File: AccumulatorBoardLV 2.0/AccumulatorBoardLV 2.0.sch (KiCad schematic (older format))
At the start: 66 parts, among them J1 Contactor 1, J10 To HV Board, J11 IMD Reset, J12 TS Interlock, J13 Temp Reset, J14 To ECU, J15 Charger LV, J16 Charger Interlock, J17 Lid Interlock, J18 From HV Board, J19 Chip 1, J2 Contactor 2, J20 Chip 2, J21 Chip 3, J22 Chip 4, J3 IMD LV, J4 BMS Connector 1, J5 BMS Connector 2, J6 BMS TX, J7 BMS RX, J8 Current Sensor, J9 BMS Reset, U1 DE1A1B-L2-12V, U10 MCP3008, U11 ISO1050, U12 stm_nucleo_FK303K8, U13 MCP3008, U14 MCP3008, U2 LM555N, U3 SN754410, U4 DE1A1B-L2-12V, U5 L78S05CV-DG, U6 DE1A1B-L2-12V, U7 DK1A1B-12V, U8 ADUM4154ARIZ, U9 MCP3008

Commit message: Began BMS slave board
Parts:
- removed C10, C11, C12, C13: 1uF, Capacitors_SMD:C_0805_HandSoldering, symbol Device:C
- removed J19: Chip 1, Connectors_Molex:Molex_NanoFit_2x05x2.50mm_Straight, symbol Connector:Conn_01x10_Male
- removed J20: Chip 2, Connectors_Molex:Molex_NanoFit_2x05x2.50mm_Straight, symbol Conn_01x10
- removed J21: Chip 3, Connectors_Molex:Molex_NanoFit_2x05x2.50mm_Straight, symbol Connector:Conn_01x10_Male
- removed J22: Chip 4, Connectors_Molex:Molex_NanoFit_2x05x2.50mm_Straight, symbol Conn_01x10
- removed R4, R5, R7, R8: R, Resistors_SMD:R_0805_HandSoldering, symbol Device:R
- removed U10, U13, U14: MCP3008, Housings_SOIC:SOIC-16_3.9x9.9mm_Pitch1.27mm, symbol MCP3008
- removed U8: ADUM4154ARIZ, Housings_SOIC:SOIC-20W_7.5x12.8mm_Pitch1.27mm, symbol FS_FINAL:ADUM4154ARIZ
- removed U9: MCP3008, Housings_SOIC:SOIC-16_3.9x9.9mm_Pitch1.27mm, symbol Analog_ADC:MCP3008
- added U?: LTC6820, symbol FS_FINAL:LTC6820
- J14: symbol Conn_01x14 -> Connector:Conn_01x14_Male
- J15: symbol Conn_01x08 -> Connector:Conn_01x08_Male
- J4: symbol Conn_01x06 -> Connector:Conn_01x06_Male
- J5: symbol Conn_01x12 -> Connector:Conn_01x12_Male
- J8: symbol Conn_01x03 -> Connector:Conn_01x03_Male
- U5: symbol L78S05CV-DG -> FS_FINAL:L78S05CV-DG
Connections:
- net labels removed: 3.3V, SCLK, TEMP_SSI, TEMP_SSO, TEMP_SS_0, TEMP_SS_1, TEMP_SS_2, TEMP_SS_3
- wire segments 88 -> 37
- no-connect marks 17 -> 8
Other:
- moved on the sheet: C6, C8, C9, J6, J7, R6, U11, U12

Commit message: updated the things
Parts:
- removed C7: 0.1uF, Capacitors_THT:C_Disc_D3.0mm_W1.6mm_P2.50mm, symbol Device:C
- removed D1, D2: D, Diodes_SMD:D_1206, symbol Device:D
- removed J13: Temp Reset, Connectors_Molex:Molex_NanoFit_1x02x2.50mm_Straight, symbol Connector:Conn_01x02_Male
- removed J18: From HV Board, Connectors_Molex:Molex_NanoFit_1x02x2.50mm_Straight, symbol Connector:Conn_01x02_Male
- removed J4: BMS Connector 1, Connectors_Molex:Molex_NanoFit_2x03x2.50mm_Straight, symbol Connector:Conn_01x06_Male
- removed J5: BMS Connector 2, Connectors_Molex:Molex_NanoFit_2x06x2.50mm_Straight, symbol Connector:Conn_01x12_Male
- removed J6: BMS TX, Connectors_Molex:Molex_NanoFit_1x02x2.50mm_Straight, symbol Connector:Conn_01x02_Male
- removed J7: BMS RX, Connectors_Molex:Molex_NanoFit_1x02x2.50mm_Straight, symbol Connector:Conn_01x02_Male
- removed U1: DE1A1B-L2-12V, FSFootprints:DE1A1B-L2-12V, symbol FS_FINAL:DE1A1B-L2-12V
- added C?: 15pF, symbol Device:C
- added C?: 10nF, symbol Device:C
- added J?: Conn_01x02_Male, symbol Connector:Conn_01x02_Male
- added L?: HM2113ZNL, symbol FS_FINAL:HM2113ZNL
- added R?: 1.5k, symbol Device:R
- added R?: 680, symbol Device:R
- added R?: 402, symbol Device:R
- added R? (x2): 22, symbol Device:R
- added R? (x2): 2.2k, symbol Device:R
- added R? (x2): 1.1k, symbol Device:R
- J14: value To ECU -> To ECU in PE Box
- R1, R2: value 1.1kR -> 1.1k
- U2: symbol LM555N -> FS_FINAL:LM555N
- U3: symbol SN754410 -> FS_FINAL:SN754410
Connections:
- net labels added: BMS_FLT_H, BMS_FLT_LAT, CHARGER_CONTROL_H, IMD_FLT_LAT, IMD_STATUS
- net labels removed: 12V, 3.3V_TS, 5V, 5V_BMS, AIRS_TEMP_OUT, BATT-, BMS_FLT_LATCHED, BMS_RX, BMS_TX, IMD_FLT_5, IMD_FLT_LATCHED, TEMP_FLT, TEMP_FLT_H, TEMP_FLT_LATCHED, TEMP_RESET, V_L, V_S
- wire segments 37 -> 71
- no-connect marks 8 -> 7
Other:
- note added: "10V to 3.3V voltage divider"
- note added: "3.3V current sensor signal"
- note added: "5V to 3.3V voltage divider"
- note added: "AIRS final to close contactors"
- note added: "AIRS from TS connector interlock to contactors"
- note added: "AIRS from charger connector interlock to charger relays"
- note added: "AIRS from lid interlock to TS connector interlock"
- note added: "AIRS from lid interlock to charger connector interlock"
- note added: "AIRS signal from PE interlocks to fault latching"
- note added: "AIRS signal from charger E-Stop to fault relays"
- note added: "AIRS to internal charger relays"
- note added: "BMS"
- note added: "BMS output to control charging"
- note added: "Fault signal from IMD"
- note added: "PWM status from IMD"
- note added: "Switched 12V to HV"
- note added: "Switched 12V to IMD"
- note added: "Unswitched 12V from Vicor DC/DC"
- note added: "V_L (deprecated)"
- note added: "V_S (deprecated)"
- note removed: "BMS CAN Termination"
- note removed: "Temp System"
- moved on the sheet: C1, C2, C3, C4, C5, C6, C8, C9, J1, J10, J11, J12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

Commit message: final lv board routed
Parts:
- removed H1, H2: MtngHole, Mounting_Holes:MountingHole_4.5mm, symbol Connector:Conn_01x01_Male
- C1, C4, C5: footprint Capacitors_THT:CP_Radial_D5.0mm_P2.50mm -> Capacitors_SMD:C_0805_HandSoldering
- C10, C7: renamed from C?; footprint (none) -> Capacitors_SMD:C_0805_HandSoldering
- C2, C3, C6, C8: footprint Capacitors_THT:C_Disc_D3.0mm_W1.6mm_P2.50mm -> Capacitors_SMD:C_0805_HandSoldering
- C9: footprint Capacitors_THT:C_Disc_D4.3mm_W1.9mm_P5.00mm -> Capacitors_SMD:C_0805_HandSoldering
- J4: renamed from J?; footprint (none) -> Connectors_Molex:Molex_NanoFit_1x02x2.50mm_Straight
- L1: renamed from L?; footprint (none) -> FSFootprints:HM2113ZNL
- R10, R11, R12, R13, R4, R5, R7, R8, R9: renamed from R?; footprint (none) -> Resistors_SMD:R_0805_HandSoldering
- U1: renamed from U?; footprint (none) -> FSFootprints:MSOP-16_[LTC6820]_10_thou_compat

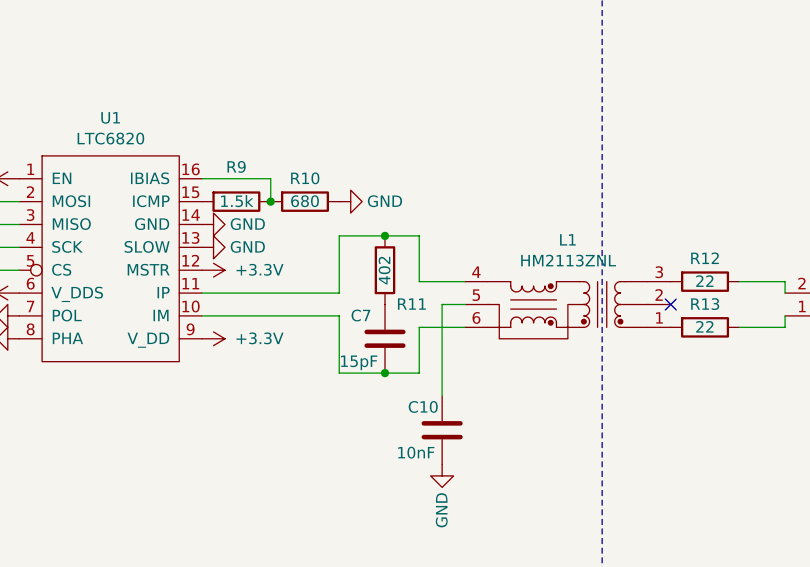
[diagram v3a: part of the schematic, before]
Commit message: Add termination resistor to isoSPI on Accumulator LV
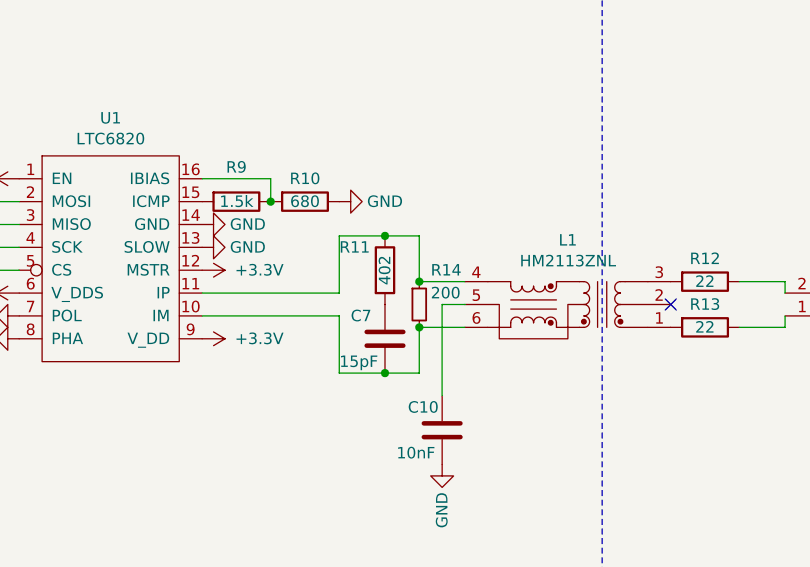
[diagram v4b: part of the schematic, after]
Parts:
- added R14: 200, Resistor_SMD:R_0805_2012Metric_Pad1.15x1.40mm_HandSolder, symbol Device:R_Small
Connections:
- net at C7.2, L1.6, U1.10 (IM): now also R14.2
- net at L1.4, R11.1, U1.11 (IP): now also R14.1
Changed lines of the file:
@@
 EESchema Schematic File Version 4
-LIBS:AccumulatorBoardLV 2.0-cache
-EELAYER 29 0
+EELAYER 26 0
 EELAYER END
 $Descr A3 16535 11693
@@
 U 1 1 5CAAC8FB
 P 8500 9050
-F 0 "R11" H 8550 8900 50  0000 L CNN
+F 0 "R11" H 8300 9150 50  0000 L CNN
 F 1 "402" V 8500 9050 50  0000 C CNN
 F 2 "Resistors_SMD:R_0805_HandSoldering" V 8430 9050 50  0001 C CNN
@@
 Text GLabel 4500 9050 0    60   Output ~ 0
 CHARGER_CONTROL
+$Comp
+L Device:R_Small R14
+U 1 1 5CABE1FF
+P 8650 9200
+F 0 "R14" H 8700 9350 50  0000 L CNN
+F 1 "200" H 8700 9250 50  0000 L CNN
+F 2 "Resistor_SMD:R_0805_2012Metric_Pad1.15x1.40mm_HandSolder" H 8650 9200 50  0001 C CNN
+F 3 "~" H 8650 9200 50  0001 C CNN
+	1    8650 9200
+	1    0    0    -1
+$EndComp
+Connection ~ 8650 9100
+Connection ~ 8650 9300
 $EndSCHEMATC

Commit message: Update the AccLV 2.0
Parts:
- C1, C3, C5, C6, C8, C9: symbol Device:CP -> CP
- C10, C2, C4, C7: symbol Device:C -> C
- D3, D4, D5, D6, D7: symbol Device:D -> D
- J1, J11, J12, J16, J17, J2, J4, J9: symbol Connector:Conn_01x02_Male -> Conn_01x02_Male
- J10: symbol Connector:Conn_01x04_Male -> Conn_01x04_Male
- J14: symbol Connector:Conn_01x14_Male -> Conn_01x14_Male
- J15: symbol Connector:Conn_01x08_Male -> Conn_01x08_Male
- J3: symbol Connector:Conn_01x06_Male -> Conn_01x06_Male
- J8: symbol Connector:Conn_01x03_Male -> Conn_01x03_Male
- L1: symbol FS_FINAL:HM2113ZNL -> HM2113ZNL
- R1, R10, R11, R12, R13, R2, R3, R4, R5, R6, R7, R8, R9: symbol Device:R -> R
- R14: symbol Device:R_Small -> R_Small
- U1: symbol FS_FINAL:LTC6820 -> LTC6820
- U11: symbol FS_FINAL:ISO1050 -> ISO1050
- U12: symbol FS_FINAL:stm_nucleo_F303K8 -> stm_nucleo_F303K8
- U2: symbol FS_FINAL:LM555N -> LM555N
- U3: symbol FS_FINAL:SN754410 -> SN754410
- U4, U6: symbol FS_FINAL:DE1A1B-L2-12V -> DE1A1B-L2-12V
- U5: symbol FS_FINAL:L78S05CV-DG -> L78S05CV-DG
- U7: symbol FS_FINAL:DK1A1B-12V -> DK1A1B-12V
